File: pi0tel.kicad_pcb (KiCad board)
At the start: 2 copper layers, 67 x 30 mm, 14 parts, among them J1 DIN-5_180degree, J2 RPi_GPIO, Q1 BSS138, U1 LM2596S-5

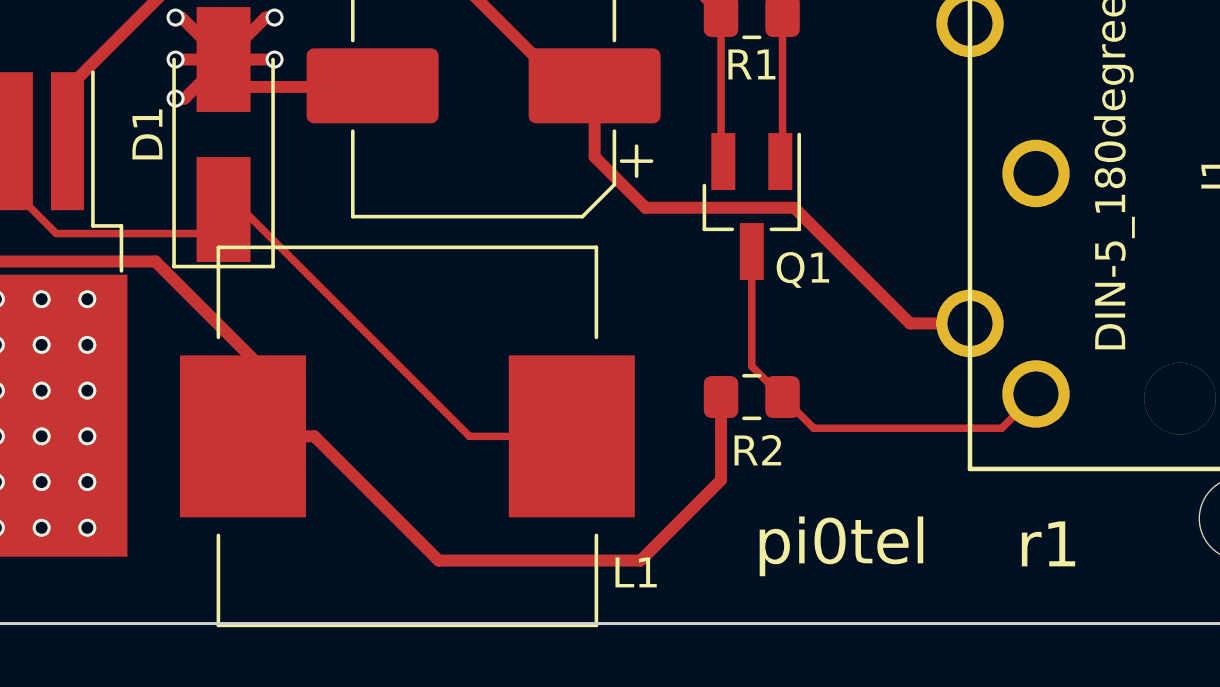
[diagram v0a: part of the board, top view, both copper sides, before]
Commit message: change inductor again now with 3D model
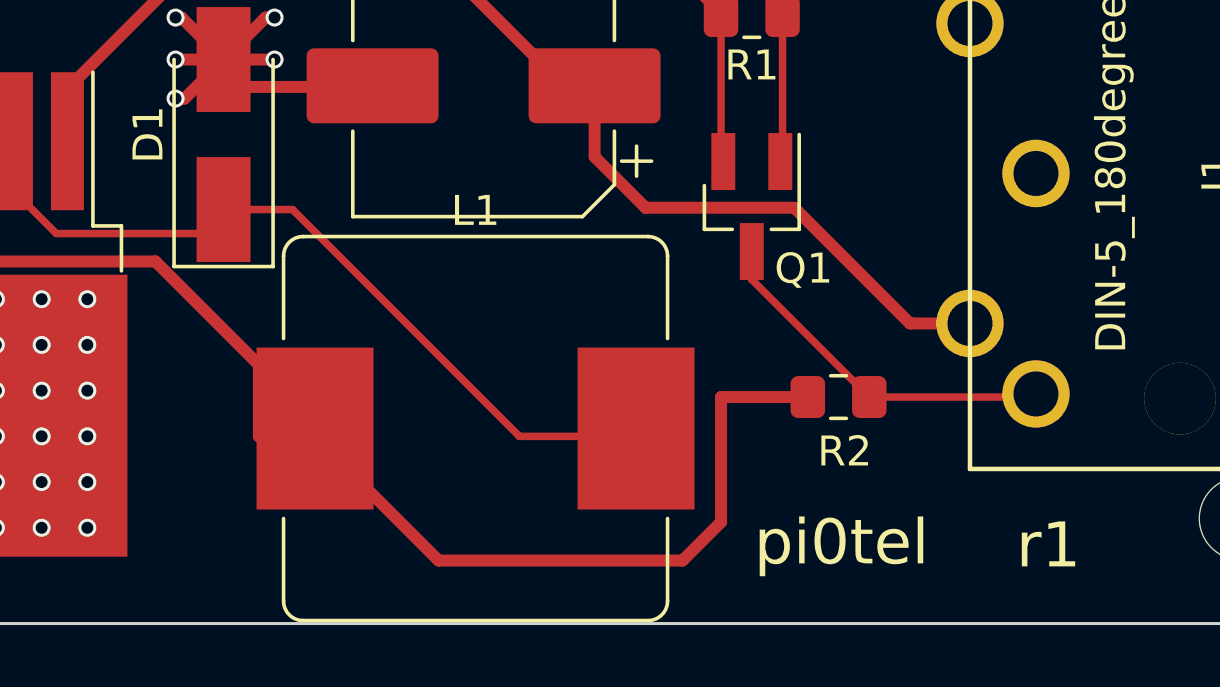
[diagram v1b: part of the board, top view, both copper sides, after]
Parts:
- L1: footprint custom:L_12x12mm_H6mm_handsolder -> Inductor_SMD:L_Bourns_SRR1260
- moved R2 2.89 mm to (60.6, 47.0)
- moved L1 2.29 mm to (48.5, 48.0)
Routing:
- net +5V: track 69.5 -> 73.2 mm
- net /MinitelTx: track 14.6 -> 12.1 mm
- net Net-(D1-Pad1): track 25.4 -> 26.0 mm
